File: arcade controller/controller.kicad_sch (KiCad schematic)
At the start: 21 parts, among them SW1 SW_DIP_x01, SW10 SW_DIP_x01, SW2 SW_DIP_x01, SW3 SW_DIP_x01, SW4 SW_DIP_x01, SW5 SW_DIP_x01, SW6 SW_DIP_x01, SW7 SW_DIP_x01, SW8 SW_DIP_x01, SW9 SW_DIP_x01

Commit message: fixed sch
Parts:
- ARCADE_PCB_CONN2: footprint Connector_Harwin:Harwin_Gecko-G125-FVX1205L0X_2x06_P1.25mm_Vertical -> Connector_PinHeader_2.54mm:PinHeader_2x06_P2.54mm_Vertical
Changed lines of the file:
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@@
 			)
 		)
-		(property "Footprint" "Connector_Harwin:Harwin_Gecko-G125-FVX1205L0X_2x06_P1.25mm_Vertical"
+		(property "Footprint" "Connector_PinHeader_2.54mm:PinHeader_2x06_P2.54mm_Vertical"
 			(at 134.62 95.25 0)
 			(effects

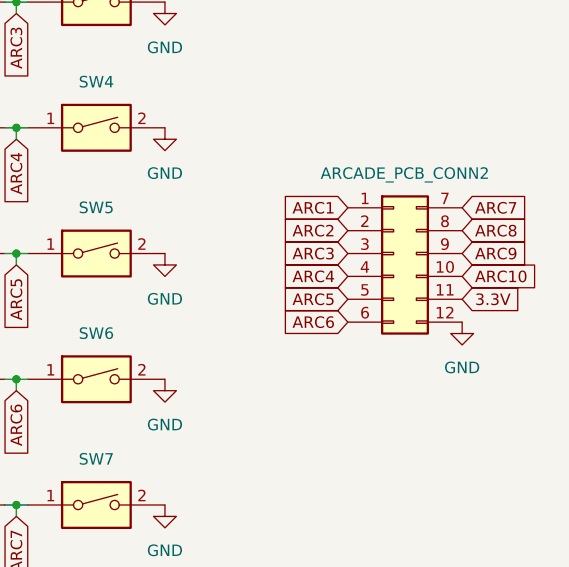
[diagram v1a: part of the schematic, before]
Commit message: wired new connector
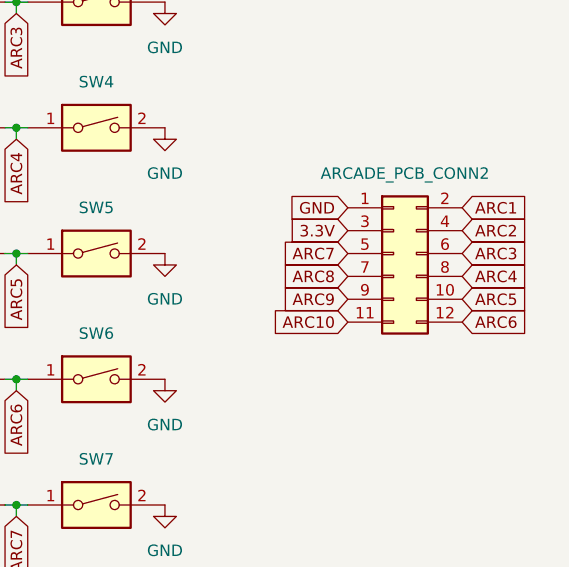
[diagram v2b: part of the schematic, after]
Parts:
- ARCADE_PCB_CONN2: value Conn_02x06_Top_Bottom -> Conn_02x06_Odd_Even
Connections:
- net 3.3V: now also ARCADE_PCB_CONN2.3 (Pin_3); no longer ARCADE_PCB_CONN2.11 (Pin_11)
- net ARC1: now also ARCADE_PCB_CONN2.2 (Pin_2); no longer ARCADE_PCB_CONN2.1 (Pin_1)
- net ARC10: now also ARCADE_PCB_CONN2.11 (Pin_11); no longer ARCADE_PCB_CONN2.10 (Pin_10)
- net ARC2: now also ARCADE_PCB_CONN2.4 (Pin_4); no longer ARCADE_PCB_CONN2.2 (Pin_2)
- net ARC3: now also ARCADE_PCB_CONN2.6 (Pin_6); no longer ARCADE_PCB_CONN2.3 (Pin_3)
- net ARC4: now also ARCADE_PCB_CONN2.8 (Pin_8); no longer ARCADE_PCB_CONN2.4 (Pin_4)
- net ARC5: now also ARCADE_PCB_CONN2.10 (Pin_10); no longer ARCADE_PCB_CONN2.5 (Pin_5)
- net ARC6: now also ARCADE_PCB_CONN2.12 (Pin_12); no longer ARCADE_PCB_CONN2.6 (Pin_6)
- net ARC7: now also ARCADE_PCB_CONN2.5 (Pin_5); no longer ARCADE_PCB_CONN2.7 (Pin_7)
- net ARC8: now also ARCADE_PCB_CONN2.7 (Pin_7); no longer ARCADE_PCB_CONN2.8 (Pin_8)
- net GND: now also ARCADE_PCB_CONN2.1 (Pin_1); no longer ARCADE_PCB_CONN2.12 (Pin_12)
